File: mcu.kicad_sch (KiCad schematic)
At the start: 27 parts, among them J301 USB_C_Receptacle_USB2.0, J302 Conn_ARM_SWD_TagConnect_TC2030, SW301 SW_SPDT, U301 STM32F413CHUx, U302 USBLC6-2SC6, Y301 12MHz

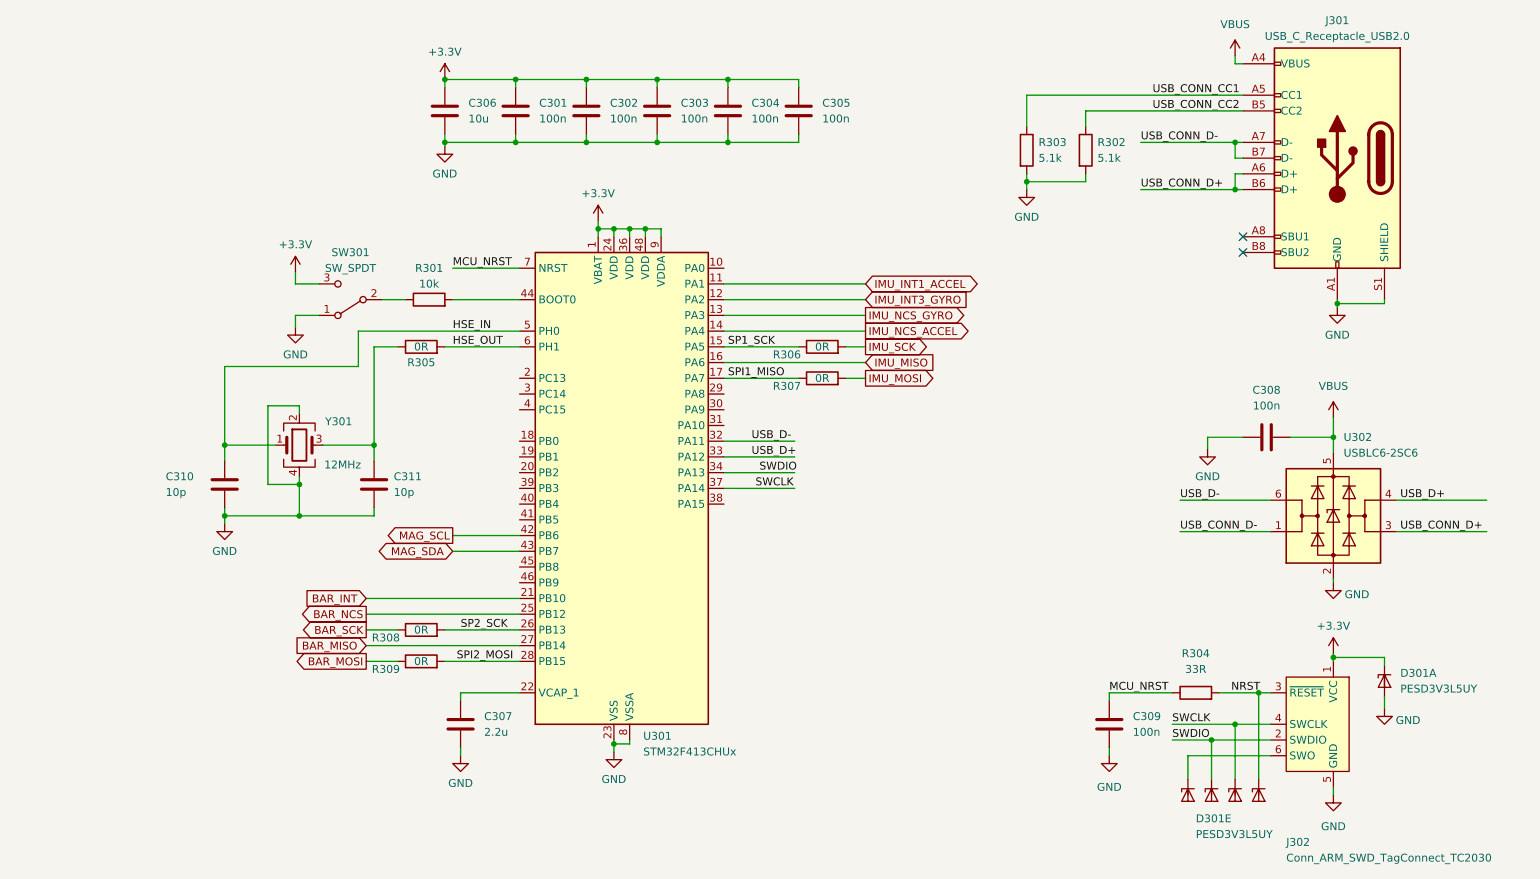
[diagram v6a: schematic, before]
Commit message: Finished connections for nrf24
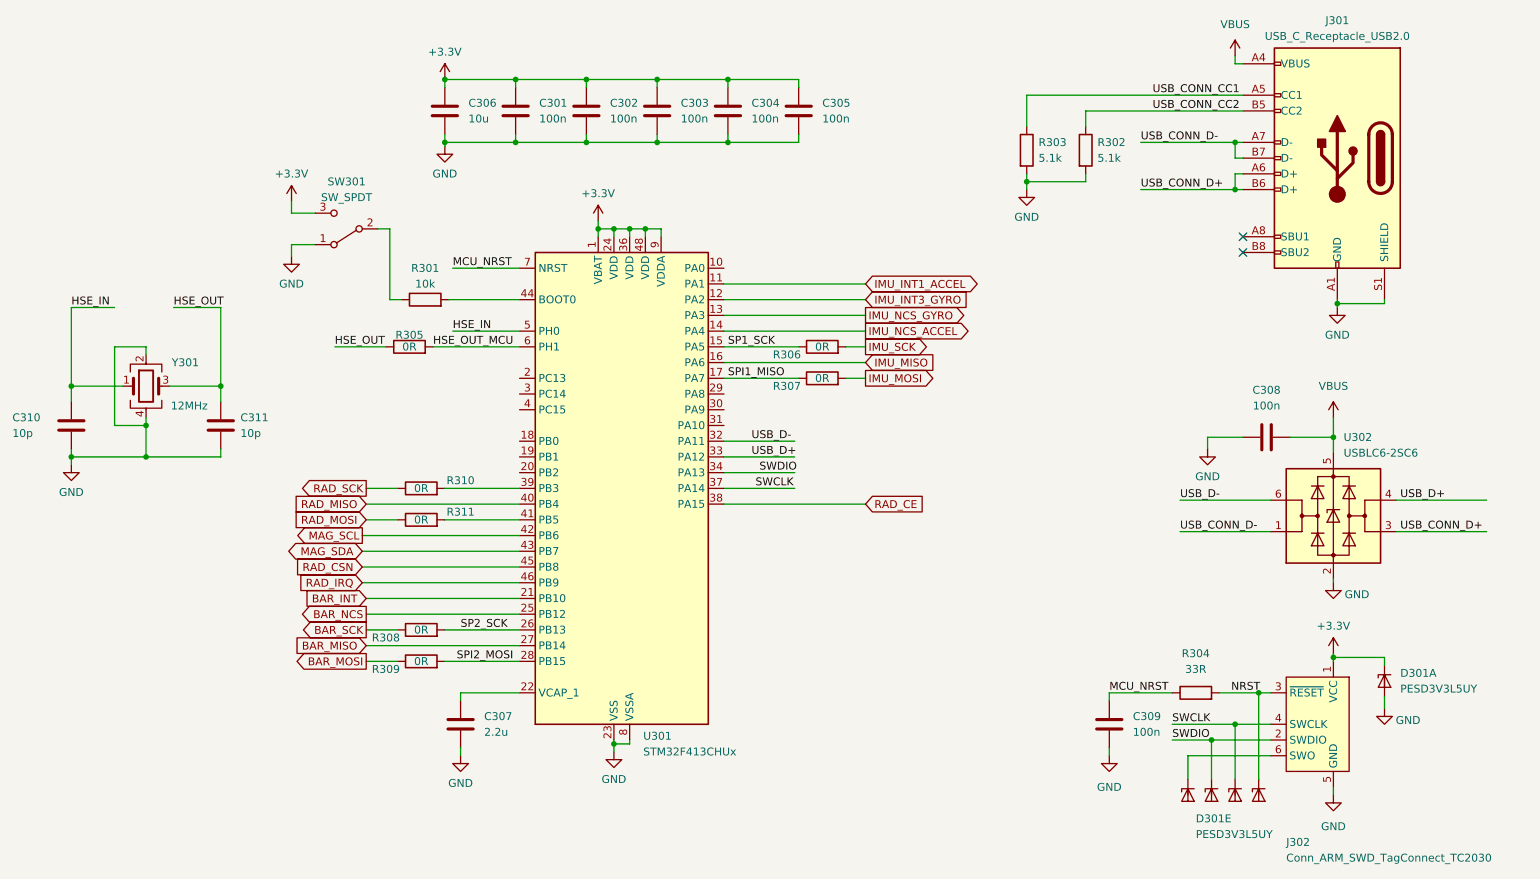
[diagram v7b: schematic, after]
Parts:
- added R310, R311: 0R, symbol Device:R
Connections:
- net HSE_OUT: now also C311.1, R305.1, Y301.3; no longer R305.2, U301.6 (PH1)
- net RAD_CE: now reaches U301.38 (PA15)
- net at U301.39 (PB3): now also R310.2
- net RAD_MISO: now reaches U301.40 (PB4)
- net at U301.41 (PB5): now also R311.2
- net RAD_CSN: now reaches U301.45 (PB8)
- net RAD_IRQ: now reaches U301.46 (PB9)
- new net HSE_OUT_MCU: R305.2, U301.6 (PH1)
- new net RAD_MOSI: R311.1
- new net RAD_SCK: R310.1
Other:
- moved on the sheet: C310, C311, R301, R305, SW301, Y301
